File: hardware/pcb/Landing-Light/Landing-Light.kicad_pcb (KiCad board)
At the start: 2 copper layers, 25 parts, among them SW1 SW_SPST, SW2 SW_SP3T, U1 BQ25172DSGR, U2 TPS61022

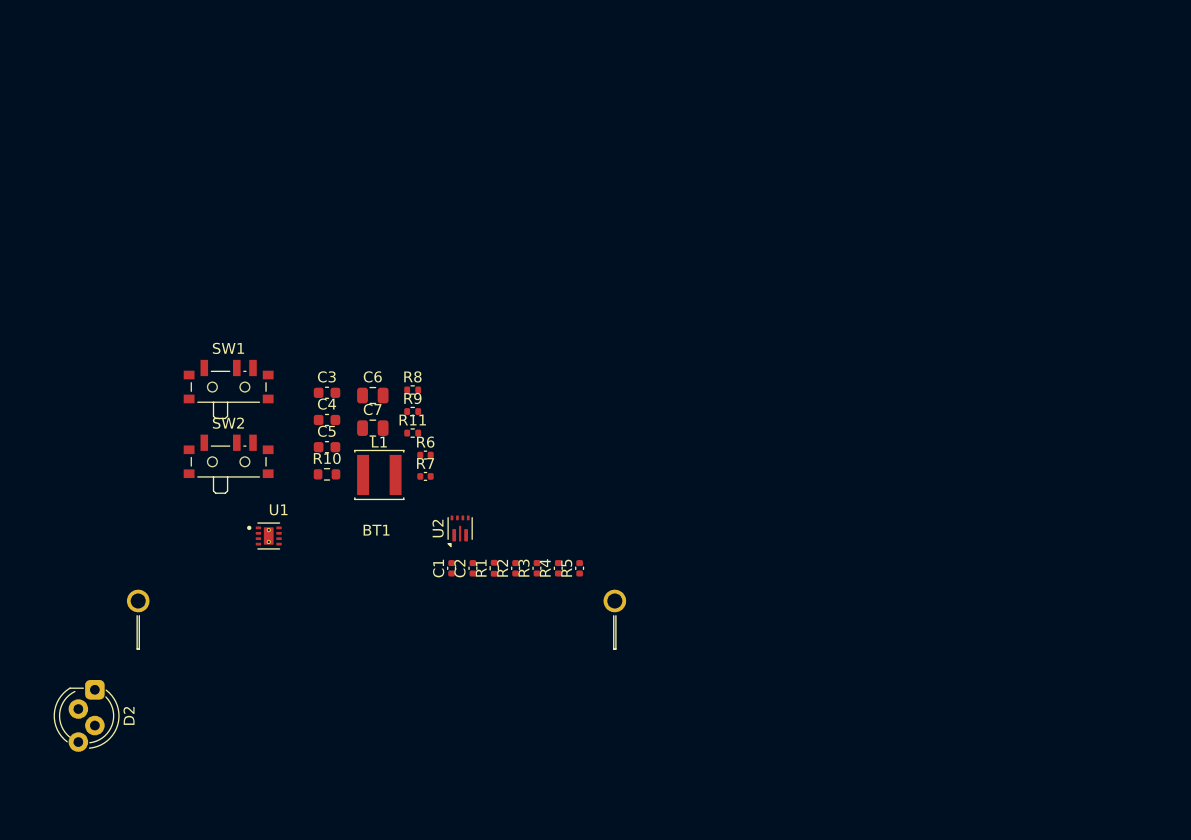
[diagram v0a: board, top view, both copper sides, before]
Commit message: Footprints complete
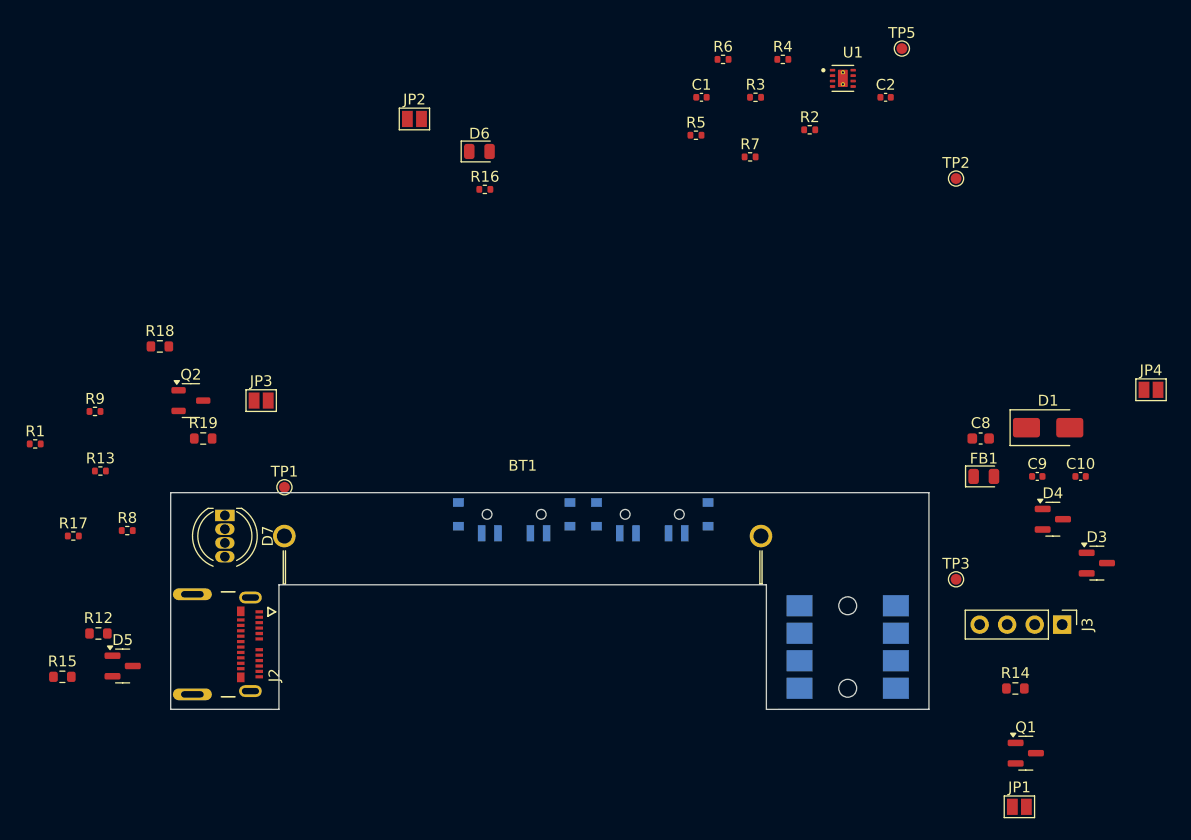
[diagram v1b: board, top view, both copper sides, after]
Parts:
- removed C3, C4, C5: 10uF, Capacitor_SMD:C_0603_1608Metric
- removed C6, C7: 22uF, Capacitor_SMD:C_0805_2012Metric
- removed D2: LED_ARGB, LED_THT:LED_D5.0mm-4_RGB_Staggered_Pins
- removed L1: L, Inductor_SMD:L_Sunlord_SWPA4030S
- removed R10: R_US, Resistor_SMD:R_0603_1608Metric
- removed R11: R_US, Resistor_SMD:R_0402_1005Metric
- removed SW1: SW_SPST, Button_Switch_SMD:SW_SPDT_PCM12
- removed U2: TPS61022, Package_DFN_QFN:Texas_RWU0007A_VQFN-7_2x2mm_P0.5mm
- added C10: 100nF, Capacitor_SMD:C_0402_1005Metric, F.Cu at (202.5, 86.5)
- added C8: 10uF, Capacitor_SMD:C_0603_1608Metric, F.Cu at (193.3, 83.0)
- added C9: 1uF, Capacitor_SMD:C_0402_1005Metric, F.Cu at (198.5, 86.5)
- added D1: Schottky, Diode_SMD:D_SMA, F.Cu at (199.5, 82.0)
- added D3: D_TVS_Dual_AAC, Package_TO_SOT_SMD:SOT-23, F.Cu at (204.0, 94.5)
- added D4: D_TVS_Dual_AAC, Package_TO_SOT_SMD:SOT-23, F.Cu at (199.9, 90.5)
- added D5: D_TVS_Dual_AAC, Package_TO_SOT_SMD:SOT-23, F.Cu at (114.1, 104.0)
- added D6: RED, LED_SMD:LED_0805_2012Metric, F.Cu at (147.0, 56.5)
- added D7: LED_RKGB, LED_THT:LED_D5.0mm-4_RGB, F.Cu at (123.5, 90.1)
- added FB1: FerriteBead, Diode_SMD:D_0805_2012Metric, F.Cu at (193.6, 86.5)
- added J1: Conn_01x04, Landing-Light:70AAJ-4-F1G, B.Cu at (181.0, 102.2)
- added J2: 2012670005, Landing-Light:MOLEX_2012670005, F.Cu at (118.7, 102.0)
- added J3: Conn_01x04, Connector_PinHeader_2.54mm:PinHeader_1x04_P2.54mm_Vertical, F.Cu at (200.8, 100.2)
- added JP1: Jumper_2_Open, Jumper:SolderJumper-2_P1.3mm_Open_Pad1.0x1.5mm, F.Cu at (196.8, 117.0)
- added JP2: Jumper_2_Open, Jumper:SolderJumper-2_P1.3mm_Open_Pad1.0x1.5mm, F.Cu at (141.0, 53.5)
- added JP3: Jumper_2_Open, Jumper:SolderJumper-2_P1.3mm_Open_Pad1.0x1.5mm, F.Cu at (126.8, 79.5)
- added JP4: Jumper_2_Open, Jumper:SolderJumper-2_P1.3mm_Open_Pad1.0x1.5mm, F.Cu at (209.0, 78.5)
- added Q1: PMOS, Package_TO_SOT_SMD:SOT-23, F.Cu at (197.4, 112.0)
- added Q2: NMOS, Package_TO_SOT_SMD:SOT-23-3, F.Cu at (120.4, 79.5)
- added R12: 5.1k, Resistor_SMD:R_0603_1608Metric, F.Cu at (111.8, 101.0)
- added R13: 330R, Resistor_SMD:R_0402_1005Metric, F.Cu at (112.0, 86.0)
- added R14: 100k, Resistor_SMD:R_0603_1608Metric, F.Cu at (196.5, 106.1)
- added R15: 5.1k, Resistor_SMD:R_0603_1608Metric, F.Cu at (108.5, 105.0)
- added R16: 330R, Resistor_SMD:R_0402_1005Metric, F.Cu at (147.5, 60.0)
- added R17: 100R, Resistor_SMD:R_0402_1005Metric, F.Cu at (109.5, 92.0)
- added R18: 100k, Resistor_SMD:R_0603_1608Metric, F.Cu at (117.5, 74.5)
- added R19: R_US, Resistor_SMD:R_0603_1608Metric, F.Cu at (121.5, 83.0)
- added SW3: SW_SPDT, Landing-Light:SSSS810201, B.Cu at (163.0, 90.0)
- added TP1: +BATT, TestPoint:TestPoint_Pad_D1.0mm, F.Cu at (129.0, 87.5)
- added TP2: VCC, TestPoint:TestPoint_Pad_D1.0mm, F.Cu at (191.0, 59.0)
- added TP3: VBUS, TestPoint:TestPoint_Pad_D1.0mm, F.Cu at (191.0, 96.0)
- added TP5: STATUS, TestPoint:TestPoint_Pad_D1.0mm, F.Cu at (186.0, 47.0)
- R1: value R_US -> 330R
- R2, R3, R4, R5, R6, R7: footprint Capacitor_SMD:C_0402_1005Metric -> Resistor_SMD:R_0402_1005Metric
- R8, R9: value R_US -> 100R
- SW2: footprint Button_Switch_SMD:SW_SPDT_PCM12 -> Landing-Light:SSSS812201; moved to B.Cu
- moved U1 67.8 mm to (180.6, 49.8)
- moved C2 57.8 mm to (184.5, 51.5), turned to 0 degrees
- moved R4 51.4 mm to (175.0, 48.0), turned to 0 degrees
- moved C1 49.2 mm to (167.5, 51.5), turned to 0 degrees
- moved R2 48.7 mm to (177.5, 54.5), turned to 0 degrees
- moved R3 47.9 mm to (172.5, 51.5), turned to 0 degrees
- moved R6 45.7 mm to (169.5, 48.0)
- moved R1 43.9 mm to (106.0, 83.5), turned to 0 degrees
- moved R7 42.1 mm to (172.0, 57.0)
- moved R5 41.4 mm to (167.0, 55.0), turned to 0 degrees
- moved R8 29.4 mm to (114.5, 91.5)
- moved R9 29.3 mm to (111.5, 80.5)
- moved SW2 26.9 mm to (150.2, 90.0)
- moved BT1 14.8 mm to (151.0, 86.0)
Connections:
- C1 pad 1: GND -> -BATT
- C2 pad 1: GND -> -BATT
- C2 pad 2: Net-(U1-OUT) -> +BATT
- R1 pad 1: Net-(D2-RK) -> Net-(R1-Pad1)
- R2 pad 2: GND -> -BATT
- R3 pad 2: GND -> -BATT
- R4 pad 2: GND -> -BATT
- R5 pad 2: GND -> -BATT
- R8 pad 1: Net-(D2-GK) -> Net-(R8-Pad1)
- R8 pad 2: Net-(R8-Pad2) -> Net-(D7-GA)
- R9 pad 1: Net-(D2-BK) -> Net-(R9-Pad1)
- SW2 pad 1: Net-(R1-Pad2) -> Net-(R9-Pad1)
- SW2 pad 2: Net-(R8-Pad2) -> Net-(R8-Pad1)
- SW2 pad 3: GND -> +3V3
- U1 pad 4: GND -> -BATT
- U1 pad 8: Net-(U1-OUT) -> +BATT
- U1 pad 9: GND -> -BATT
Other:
- board outline added: 70 x 20 mm

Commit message: Changing to new layout
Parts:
- removed D5: D_TVS_Dual_AAC, Package_TO_SOT_SMD:SOT-23
- removed J3: Conn_01x04, Connector_PinHeader_2.54mm:PinHeader_1x04_P2.54mm_Vertical
- removed TP1: +BATT, TestPoint:TestPoint_Pad_D1.0mm
- added C11: 10uF, Capacitor_SMD:C_0603_1608Metric, F.Cu at (157.0, 74.3)
- added C12: 10uF, Capacitor_SMD:C_0603_1608Metric, F.Cu at (157.0, 76.8)
- added C13: 100nF, Capacitor_SMD:C_0402_1005Metric, F.Cu at (165.8, 77.1)
- added D2: D_TVS_Dual_AAC, Package_TO_SOT_SMD:SOT-23, F.Cu at (135.7, 94.5)
- added L2: 2.2uH, Inductor_SMD:L_Sunlord_SWPA3015S, F.Cu at (166.2, 80.8)
- added R20: R_US, Resistor_SMD:R_0603_1608Metric, F.Cu at (157.0, 79.4)
- added R21: R_US, Resistor_SMD:R_0603_1608Metric, F.Cu at (157.0, 81.9)
- added TP6: +3V3, TestPoint:TestPoint_Pad_D1.0mm, F.Cu at (165.9, 74.6)
- added U3: TPS61200DRC, Package_SON:Texas_S-PVSON-N10_ThermalVias, F.Cu at (161.7, 75.8)
- moved JP4 38.1 mm to (176.0, 97.6), turned to 90 degrees
- moved R1 36.2 mm to (140.9, 93.1), turned to 180 degrees
- moved R18 35.1 mm to (146.5, 94.2), turned to -90 degrees
- moved R9 33.1 mm to (140.9, 95.6), turned to 180 degrees
- moved R19 32.5 mm to (152.0, 94.2), turned to 90 degrees
- moved Q2 32.3 mm to (149.2, 93.9), turned to -90 degrees
- moved D1 31.8 mm to (176.2, 103.6), turned to -90 degrees
- moved R17 29.6 mm to (138.9, 95.6), turned to 180 degrees
- moved C10 29.3 mm to (179.1, 104.1), turned to -90 degrees
- moved R13 27.9 mm to (138.9, 93.1), turned to 180 degrees
- moved C1 26.8 mm to (176.5, 76.8)
- moved C2 26.8 mm to (193.5, 76.8)
- moved R2 26.8 mm to (186.5, 79.8)
- moved R3 26.8 mm to (181.5, 76.8)
- moved R4 26.8 mm to (184.0, 73.2)
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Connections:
- C8 pad 1: VBUS -> VSS
- C9 pad 2: VBUS -> VSS
- FB1 pad 1: VBUS -> VSS
- J1 pad 4: VBUS -> VSS
- J2 pad A4: VBUS -> VSS
- J2 pad A9: VBUS -> VSS
- J2 pad B4: VBUS -> VSS
- J2 pad B9: VBUS -> VSS
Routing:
- added copper zone on B.Cu, net -BATT
- added copper zone on F.Cu, net -BATT
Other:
- outline, holes or cut-outs redrawn

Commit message: Tidying up layout
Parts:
- moved R16 40.7 mm to (185.3, 93.9), turned to 180 degrees
- moved D6 40.4 mm to (182.5, 94.4), turned to 180 degrees
- moved JP2 39.3 mm to (179.2, 94.4), turned to 180 degrees
- moved TP5 24.3 mm to (187.5, 95.4)
- moved TP2 21.3 mm to (182.6, 96.6)
- moved TP6 19.8 mm to (160.9, 93.7), turned to 180 degrees
- moved R4 19.0 mm to (178.7, 91.4), turned to -90 degrees
- moved R6 18.2 mm to (177.6, 91.4), turned to -90 degrees
- moved U1 17.9 mm to (181.8, 91.1)
- moved C12 17.5 mm to (166.9, 91.3), turned to -90 degrees
- moved C11 17.1 mm to (159.8, 91.2), turned to 90 degrees
- moved C2 16.5 mm to (182.8, 89.3)
- moved C13 15.2 mm to (161.1, 91.6), turned to 90 degrees
- moved U3 15.1 mm to (163.8, 90.7), turned to 90 degrees
- moved R3 15.1 mm to (184.9, 91.4), turned to -90 degrees
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
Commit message: Routing complete
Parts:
- removed D1: Schottky, Diode_SMD:D_SMA
- removed JP1, JP4: Jumper_2_Open, Jumper:SolderJumper-2_P1.3mm_Open_Pad1.0x1.5mm
- removed Q1: PMOS, Package_TO_SOT_SMD:SOT-23
- removed R14: 100k, Resistor_SMD:R_0603_1608Metric
- removed R21: R_US, Resistor_SMD:R_0603_1608Metric
- added C3: 47uF, Capacitor_SMD:C_0603_1608Metric, F.Cu at (161.4, 91.1)
- added JP5: Jumper_2_Open, Jumper:SolderJumper-2_P1.3mm_Open_RoundedPad1.0x1.5mm, F.Cu at (135.0, 94.8)
- added JP6: Jumper_2_Open, Jumper:SolderJumper-2_P1.3mm_Open_RoundedPad1.0x1.5mm, B.Cu at (154.1, 91.8)
- added Q3: NMOS, Package_TO_SOT_SMD:SOT-23-3, F.Cu at (131.5, 94.8)
- added Q4: PMOS, Package_TO_SOT_SMD:SOT-23, F.Cu at (154.6, 94.3)
- added R10: 1M, Resistor_SMD:R_0603_1608Metric, F.Cu at (160.6, 88.8)
- added R11: 180k, Resistor_SMD:R_0603_1608Metric, F.Cu at (163.7, 88.8)
- added TP1: VCC, TestPoint:TestPoint_Pad_D1.0mm, B.Cu at (173.0, 89.5)
- added TP4: -BATT, TestPoint:TestPoint_Pad_D1.0mm, B.Cu at (126.5, 92.0)
- added TP7: VIN, TestPoint:TestPoint_Pad_D1.0mm, B.Cu at (176.2, 96.0)
- JP2, JP3: footprint Jumper:SolderJumper-2_P1.3mm_Open_Pad1.0x1.5mm -> Jumper:SolderJumper-2_P1.3mm_Open_RoundedPad1.0x1.5mm; moved to B.Cu
- R19: value R_US -> 0R
- R20: value R_US -> 100k
- SW2, SW3: moved to F.Cu
- TP2: value VCC -> 5V; moved to B.Cu
- TP3: value VBUS -> GND; moved to B.Cu
- TP5, TP6: moved to B.Cu
- moved TP3 58.9 mm to (126.5, 94.2), turned to 180 degrees
- moved TP6 9.40 mm to (152.8, 89.0), turned to 0 degrees
- moved TP5 9.19 mm to (180.3, 89.6), turned to 180 degrees
- moved R5 8.78 mm to (177.2, 92.8), turned to 90 degrees
- moved R6 7.96 mm to (185.5, 92.8), turned to 90 degrees
- moved R3 6.79 mm to (178.2, 92.8), turned to 90 degrees
- moved R17 6.60 mm to (128.3, 90.0)
- moved R9 6.60 mm to (130.3, 90.0)
- moved D4 6.43 mm to (185.9, 99.0), turned to 0 degrees
- moved C2 6.19 mm to (180.4, 95.0), turned to 180 degrees
- moved R4 5.97 mm to (184.5, 92.8), turned to 90 degrees
- moved C1 5.89 mm to (182.3, 95.0), turned to 0 degrees
- moved R1 5.77 mm to (130.3, 88.5)
- moved R13 5.77 mm to (128.3, 88.5)
- moved JP2 5.49 mm to (184.6, 93.4), turned to -90 degrees
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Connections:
- net Net-(U3-VAUX) renamed VAUX
- C1 pad 1: -BATT -> GND
- C1 pad 2: VBUS -> +5V
- C10 pad 1: VBUS -> +5V
- C10 pad 2: -BATT -> GND
- C11 pad 2: -BATT -> GND
- C12 pad 1: VCC -> +BATT
- C12 pad 2: -BATT -> GND
- C13 pad 2: -BATT -> GND
- C2 pad 1: -BATT -> GND
- C8 pad 1: VSS -> VIN
- C8 pad 2: -BATT -> GND
- C9 pad 1: -BATT -> GND
- C9 pad 2: VSS -> VIN
- D2 pad 3: -BATT -> GND
- D3 pad 3: -BATT -> GND
- D4 pad 2: VBUS -> VIN
- D4 pad 3: -BATT -> GND
- FB1 pad 1: VSS -> VIN
- FB1 pad 2: VBUS -> +5V
- J1 pad 1: -BATT -> GND
- J1 pad 4: VSS -> VIN
- J2 pad A1: -BATT -> GND
- J2 pad A12: -BATT -> GND
- J2 pad A4: VSS -> VIN
- J2 pad A9: VSS -> VIN
- J2 pad B1: -BATT -> GND
- J2 pad B12: -BATT -> GND
- J2 pad B4: VSS -> VIN
- J2 pad B9: VSS -> VIN
- JP2 pad 2: VBUS -> +5V
- L2 pad 1: VCC -> +BATT
- Q2 pad 2: VBUS -> +5V
- R12 pad 1: -BATT -> GND
- R15 pad 2: -BATT -> GND
- R18 pad 1: VBUS -> +5V
- R18 pad 2: -BATT -> GND
- R19 pad 2: -BATT -> GND
- R2 pad 2: -BATT -> GND
- R20 pad 1: +3V3 -> +5V
- R20 pad 2: Net-(U3-FB) -> GND
- R3 pad 2: -BATT -> GND
- R4 pad 2: -BATT -> GND
- R5 pad 2: -BATT -> GND
- SW3 pad 1: -BATT -> Net-(JP6-A)
- TP2 pad 1: VCC -> +5V
- TP3 pad 1: VBUS -> GND
- U1 pad 1: VBUS -> +5V
- U1 pad 4: -BATT -> GND
- U1 pad 9: -BATT -> GND
- U3 pad 11: -BATT -> GND
- U3 pad 4: -BATT -> GND
- U3 pad 5: VCC -> +BATT
- U3 pad 6: VCC -> +BATT
- U3 pad 7: VCC -> +BATT
- U3 pad 8: VCC -> +BATT
- U3 pad 9: -BATT -> GND
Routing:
- net VIN: track 0.00 -> 81.4 mm, vias 0 -> 2
- net +5V: track 0.00 -> 53.4 mm, vias 0 -> 3
- net GND: track 0.00 -> 47.5 mm, vias 0 -> 19
- net VAUX: track 0.00 -> 40.4 mm, vias 0 -> 2
- net Net-(D7-K): track 0.00 -> 31.2 mm, vias 0 -> 2
- net +3V3: track 0.00 -> 31.0 mm, vias 0 -> 4
- net CHARGE_STATUS: track 0.00 -> 30.4 mm, vias 0 -> 2
- net /CC1: track 0.00 -> 28.6 mm, vias 0 -> 2
- net /CC2: track 0.00 -> 27.4 mm, vias 0 -> 2
- net +BATT: track 0.00 -> 17.5 mm, vias 0 -> 2
- net Net-(R9-Pad1): track 0.00 -> 13.5 mm
- net -BATT: track 0.00 -> 10.7 mm
- net Net-(R8-Pad1): track 0.00 -> 10.3 mm
- net DATA2: track 0.00 -> 10.0 mm, vias 0 -> 1
- net Net-(D7-GA): track 0.00 -> 9.76 mm
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- added copper zone on F.Cu, net +3V3
- added copper zone on F.Cu, net +BATT
- added copper zone on B.Cu, net GND
- added copper zone on F.Cu, net GND
- removed copper zone on B.Cu, net -BATT
- removed copper zone on F.Cu, net -BATT
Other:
- outline, holes or cut-outs redrawn
- board text added: "-"
- board text added: "3V3"
- board text added: "5V"
- board text added: "B"
- board text added: "BATT-"
- board text added: "CHRG"
- board text added: "CHRG LED"
- board text added: "G"
- board text added: "GND"
- board text added: "NMOS"
- board text added: "PMOS"
- board text added: "R"
- board text added: "REV"
- board text added: "VIN"

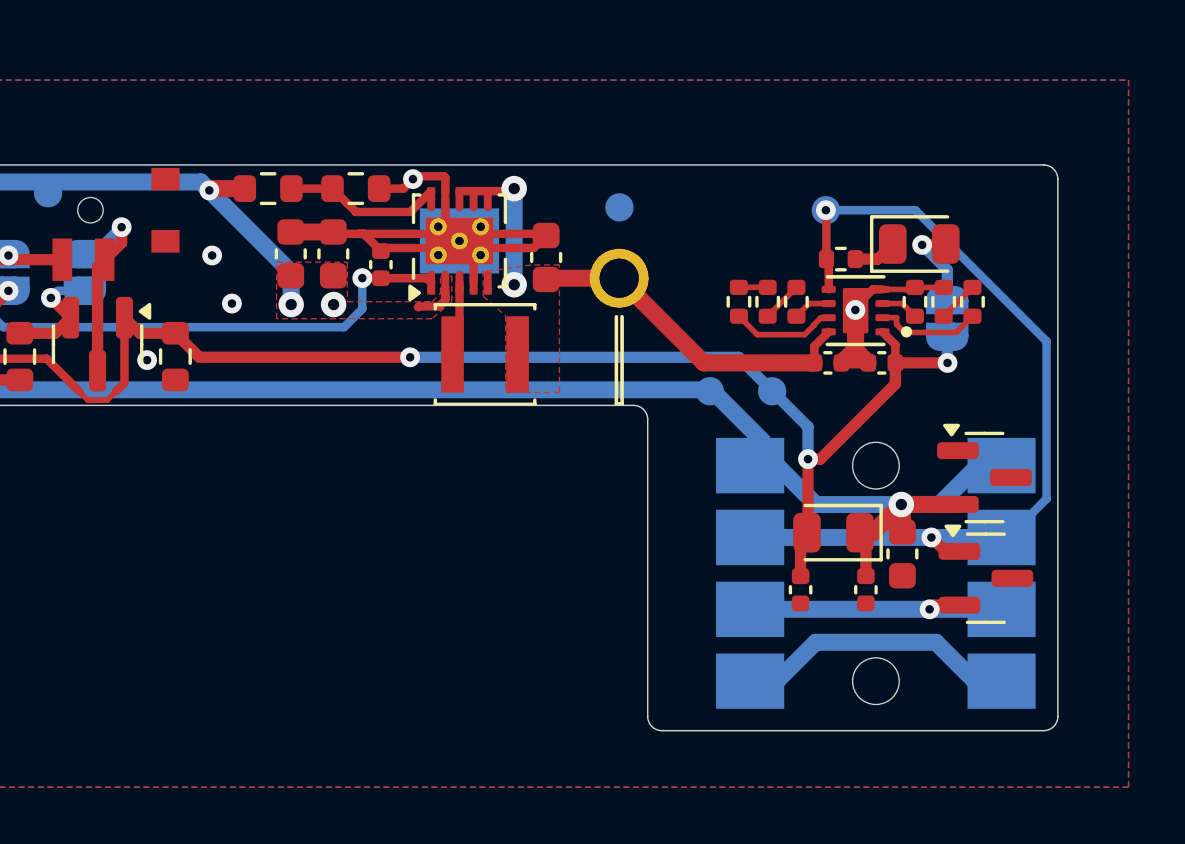
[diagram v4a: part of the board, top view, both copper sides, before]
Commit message: Tidy resistor values
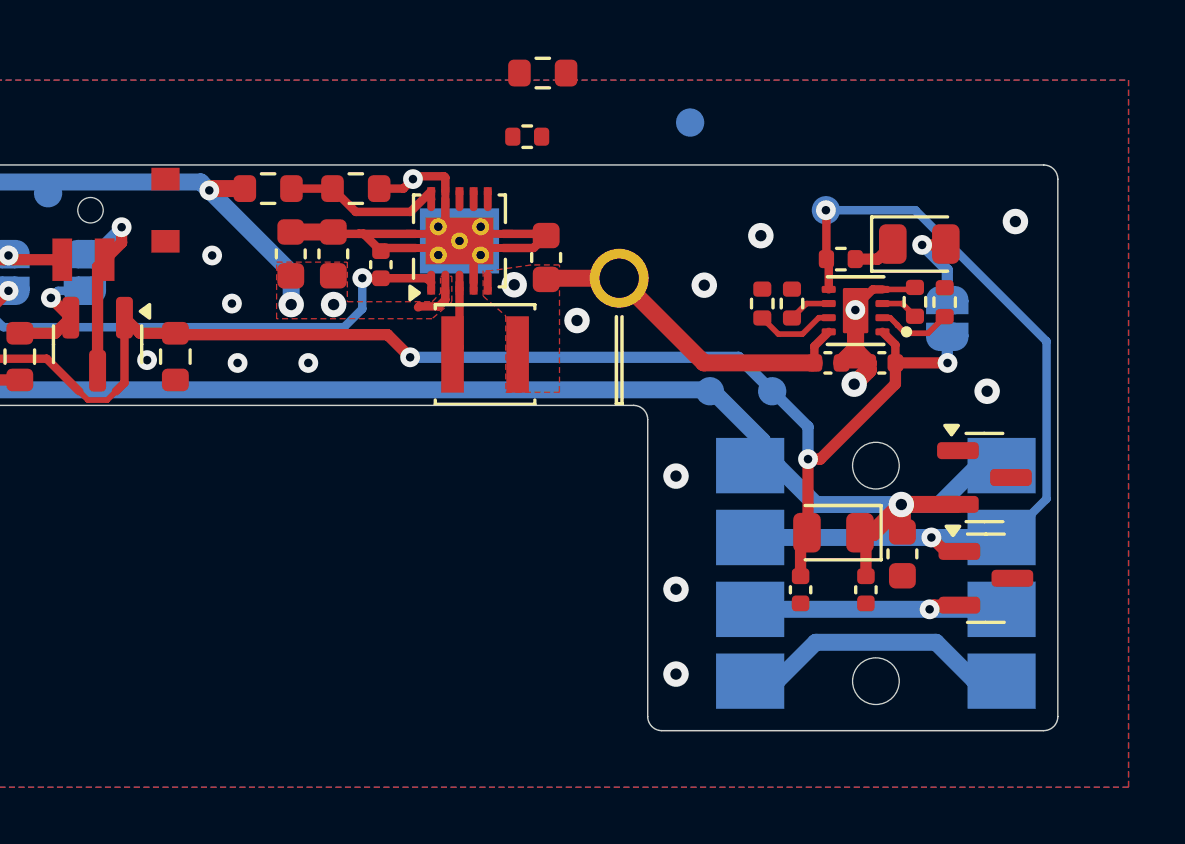
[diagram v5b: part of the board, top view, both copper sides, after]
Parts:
- R3: value 3.3k -> 180k; footprint Resistor_SMD:R_0402_1005Metric -> Resistor_SMD:R_0603_1608Metric
- R4: value 330R -> 470k
- R6: value 470R -> 1.5k
- R7: value 33k -> 27k
- moved R4 15.8 mm to (169.7, 87.0), turned to 0 degrees
- moved R3 11.3 mm to (170.3, 84.8), turned to 0 degrees
- moved TP1 3.91 mm to (175.5, 86.5)
- moved R6 0.98 mm to (184.5, 92.8)
- moved R5 0.83 mm to (178.1, 92.9)
- moved R7 0.17 mm to (179.1, 92.9)
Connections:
- R3 pad 1: Net-(R3-Pad1) -> unconnected-(R3-Pad1)
- R3 pad 2: GND -> unconnected-(R3-Pad2)
- R4 pad 1: Net-(R4-Pad1) -> unconnected-(R4-Pad1)
- R4 pad 2: GND -> unconnected-(R4-Pad2)
- R6 pad 2: Net-(R4-Pad1) -> GND
- R7 pad 2: Net-(R3-Pad1) -> GND
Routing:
- net +BATT: track 17.5 -> 12.1 mm, vias 2 -> 1
- net Net-(R4-Pad1): track 1.44 -> 0.00 mm
- net Net-(R3-Pad1): track 1.44 -> 0.00 mm
- net Net-(U1-ISET): track 3.77 -> 2.68 mm
- net GND: track 47.5 -> 46.4 mm, vias 19 -> 30
- net Net-(U1-VSET): track 3.70 -> 2.83 mm
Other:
- board text added: "BATT+"
